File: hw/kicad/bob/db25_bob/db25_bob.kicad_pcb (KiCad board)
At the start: 2 copper layers, 4 parts, among them J1 DB25, U1 ADuM1200WU, U2 ADuM1200WU, U3 ADuM1200WU

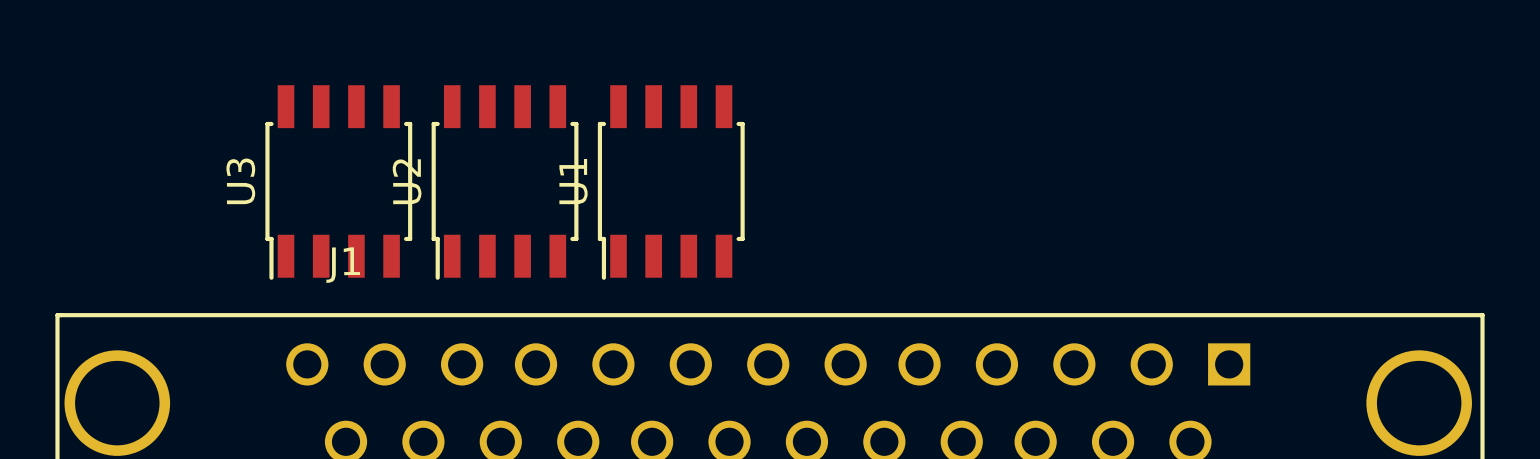
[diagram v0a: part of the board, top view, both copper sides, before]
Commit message: Added more isolators.
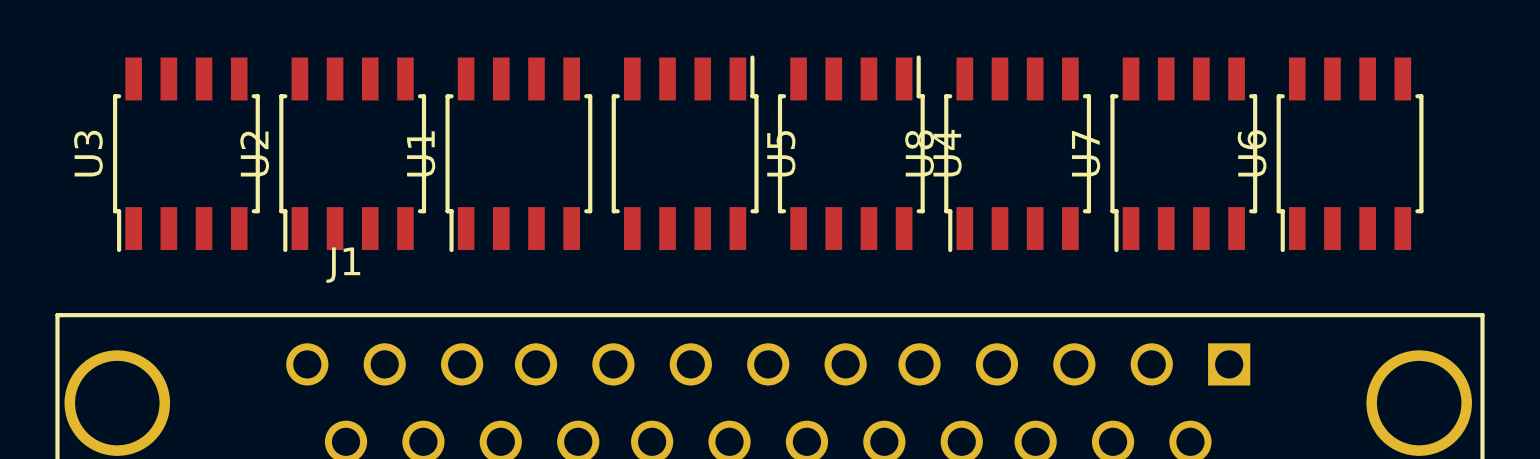
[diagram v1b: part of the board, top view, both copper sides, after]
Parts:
- added U4: ADuM1200WU, Housings_SOIC:SOIC-8_3.9x4.9mm_Pitch1.27mm, F.Cu at (154.0, 123.0)
- added U5: ADuM1200WU, Housings_SOIC:SOIC-8_3.9x4.9mm_Pitch1.27mm, F.Cu at (148.0, 123.0)
- added U6: ADuM1201WT, Housings_SOIC:SOIC-8_3.9x4.9mm_Pitch1.27mm, F.Cu at (172.0, 123.0)
- added U7: ADuM1201WT, Housings_SOIC:SOIC-8_3.9x4.9mm_Pitch1.27mm, F.Cu at (166.0, 123.0)
- added U8: ADuM1201WT, Housings_SOIC:SOIC-8_3.9x4.9mm_Pitch1.27mm, F.Cu at (160.0, 123.0)
- moved U1 5.59 mm to (142.0, 123.0)
- moved U2 5.59 mm to (136.0, 123.0)
- moved U3 5.59 mm to (130.0, 123.0)
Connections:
- U1 pad 5: Net-(U1-Pad5) -> GNDA
- U1 pad 8: Net-(U1-Pad8) -> +5VA
- U2 pad 5: Net-(U2-Pad5) -> GNDA
- U2 pad 8: Net-(U2-Pad8) -> +5VA
- U3 pad 5: Net-(U3-Pad5) -> GNDA
- U3 pad 8: Net-(U3-Pad8) -> +5VA

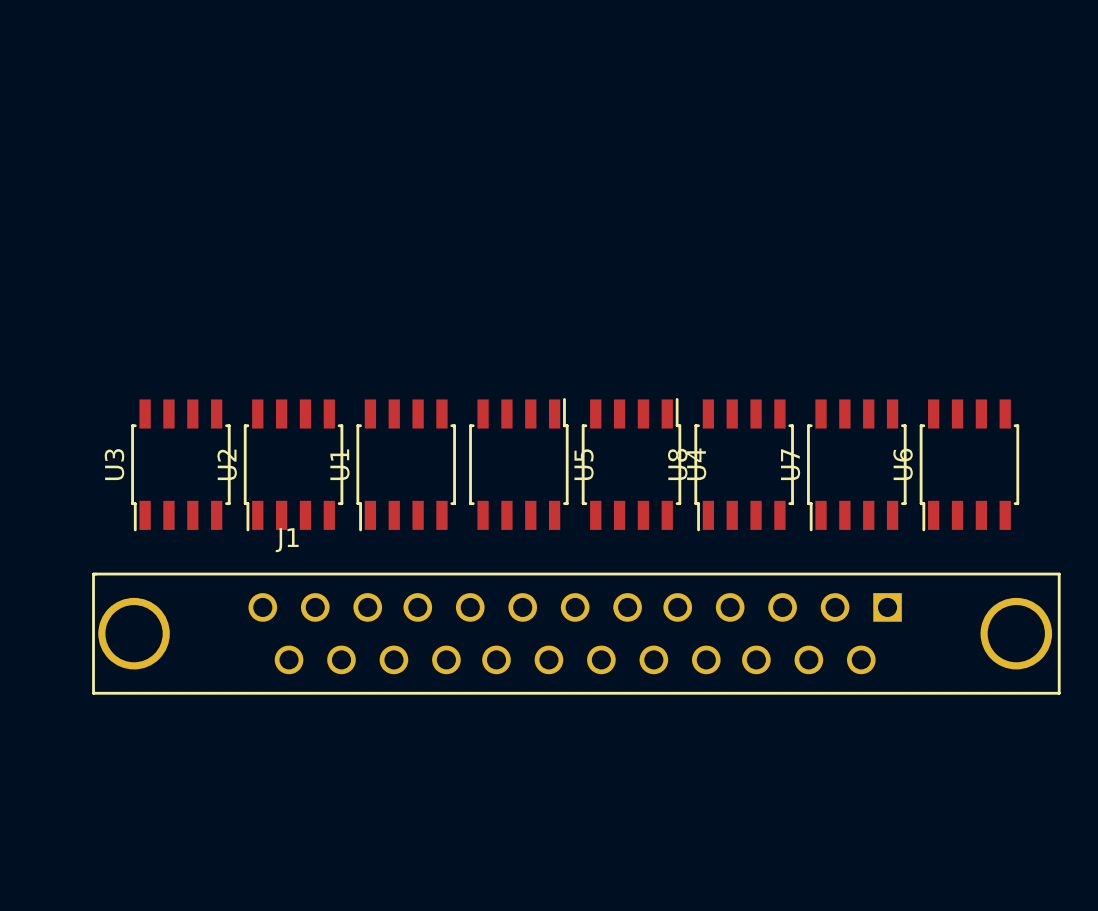
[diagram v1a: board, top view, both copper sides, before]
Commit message: Changed schematic to current feature set.
The bob will use two connections to the Mesa hardware and break out 5 SSerial
connections, 4 ABZ encoder interfaces, 5 inputs and 5 outputs.
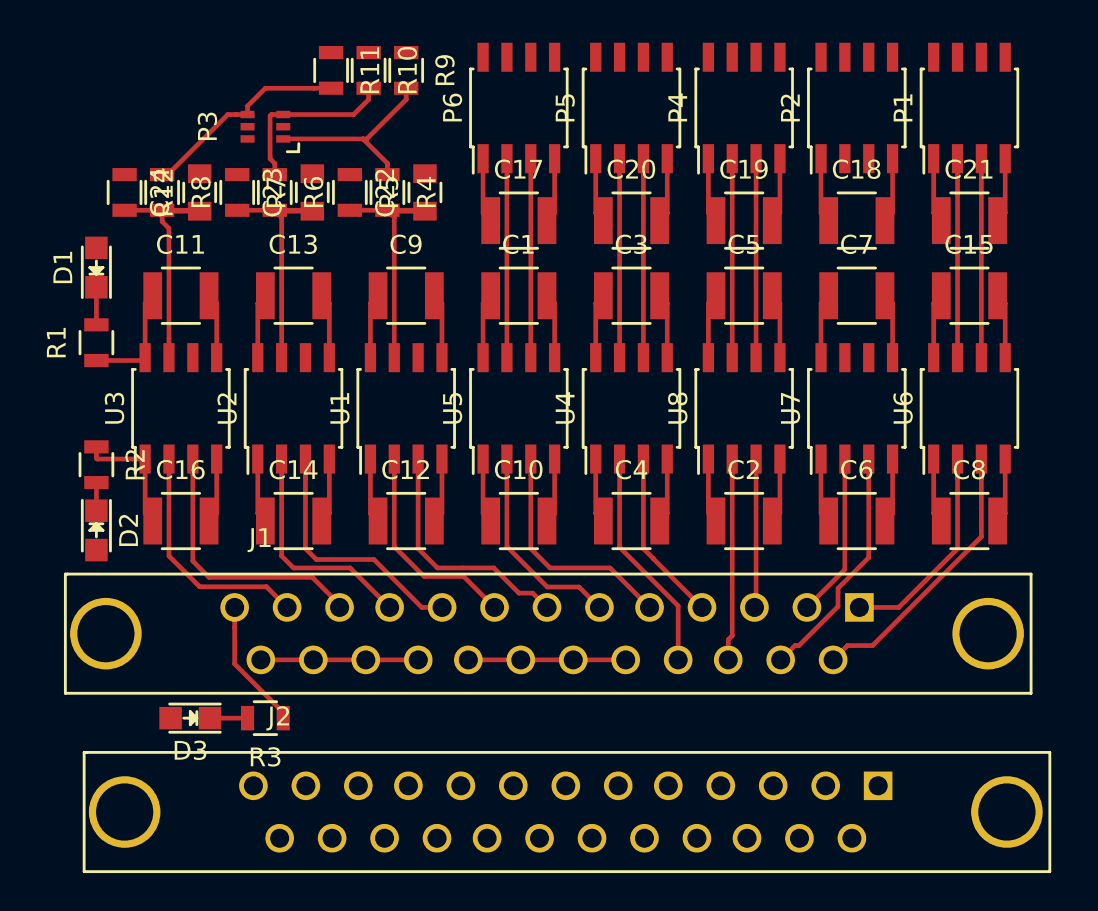
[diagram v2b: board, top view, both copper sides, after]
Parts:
- added C1: C, Capacitors_SMD:C_1210, F.Cu at (148.0, 114.0)
- added C10: C, Capacitors_SMD:C_1210, F.Cu at (148.0, 126.0)
- added C11: C, Capacitors_SMD:C_1210, F.Cu at (130.0, 114.0)
- added C12: C, Capacitors_SMD:C_1210, F.Cu at (142.0, 126.0)
- added C13: C, Capacitors_SMD:C_1210, F.Cu at (136.0, 114.0)
- added C14: C, Capacitors_SMD:C_1210, F.Cu at (136.0, 126.0)
- added C15: C, Capacitors_SMD:C_1210, F.Cu at (172.0, 114.0)
- added C16: C, Capacitors_SMD:C_1210, F.Cu at (130.0, 126.0)
- added C17: C, Capacitors_SMD:C_1210, F.Cu at (148.0, 110.0)
- added C18: C, Capacitors_SMD:C_1210, F.Cu at (166.0, 110.0)
- added C19: C, Capacitors_SMD:C_1210, F.Cu at (160.0, 110.0)
- added C2: C, Capacitors_SMD:C_1210, F.Cu at (160.0, 126.0)
- added C20: C, Capacitors_SMD:C_1210, F.Cu at (154.0, 110.0)
- added C21: C, Capacitors_SMD:C_1210, F.Cu at (172.0, 110.0)
- added C22: C, Capacitors_SMD:C_0805, F.Cu at (143.0, 108.5)
- added C23: C, Capacitors_SMD:C_0805, F.Cu at (137.0, 108.5)
- added C24: C, Capacitors_SMD:C_0805, F.Cu at (131.0, 108.5)
- added C3: C, Capacitors_SMD:C_1210, F.Cu at (154.0, 114.0)
- added C4: C, Capacitors_SMD:C_1210, F.Cu at (154.0, 126.0)
- added C5: C, Capacitors_SMD:C_1210, F.Cu at (160.0, 114.0)
- added C6: C, Capacitors_SMD:C_1210, F.Cu at (166.0, 126.0)
- added C7: C, Capacitors_SMD:C_1210, F.Cu at (166.0, 114.0)
- added C8: C, Capacitors_SMD:C_1210, F.Cu at (172.0, 126.0)
- added C9: C, Capacitors_SMD:C_1210, F.Cu at (142.0, 114.0)
- added D1: LED, LEDs:LED-0805, F.Cu at (125.5, 112.5)
- added D2: LED, LEDs:LED-0805, F.Cu at (125.5, 126.5)
- added D3: LED, LEDs:LED-0805, F.Cu at (130.5, 136.5)
- added J2: DB25, Connect:DB25FD, F.Cu at (150.5, 141.5)
- added P1: DIL8, Housings_SOIC:SOIC-8_3.9x4.9mm_Pitch1.27mm, F.Cu at (172.0, 104.0)
- added P2: DIL8, Housings_SOIC:SOIC-8_3.9x4.9mm_Pitch1.27mm, F.Cu at (166.0, 104.0)
- added P3: DIL6, Housings_SOT-23_SOT-143_TSOT-6:SC-70-6, F.Cu at (134.5, 105.0)
- added P4: DIL8, Housings_SOIC:SOIC-8_3.9x4.9mm_Pitch1.27mm, F.Cu at (160.0, 104.0)
- added P5: DIL8, Housings_SOIC:SOIC-8_3.9x4.9mm_Pitch1.27mm, F.Cu at (154.0, 104.0)
- added P6: DIL8, Housings_SOIC:SOIC-8_3.9x4.9mm_Pitch1.27mm, F.Cu at (148.0, 104.0)
- added R1: R, Resistors_SMD:R_0805, F.Cu at (125.5, 116.5)
- added R10: R, Resistors_SMD:R_0805, F.Cu at (140.0, 102.0)
- added R11: R, Resistors_SMD:R_0805, F.Cu at (138.0, 102.0)
- added R12: R, Resistors_SMD:R_0805, F.Cu at (127.0, 108.5)
- added R2: R, Resistors_SMD:R_0805, F.Cu at (125.5, 123.0)
- added R3: R, Resistors_SMD:R_0805, F.Cu at (134.5, 136.5)
- added R4: R, Resistors_SMD:R_0805, F.Cu at (141.0, 108.5)
- added R5: R, Resistors_SMD:R_0805, F.Cu at (139.0, 108.5)
- added R6: R, Resistors_SMD:R_0805, F.Cu at (135.0, 108.5)
- added R7: R, Resistors_SMD:R_0805, F.Cu at (133.0, 108.5)
- added R8: R, Resistors_SMD:R_0805, F.Cu at (129.0, 108.5)
- added R9: R, Resistors_SMD:R_0805, F.Cu at (142.0, 102.0)
- U1, U2, U3, U4, U5: value ADuM1200WU -> ADuM1201WT
- moved U1 3.00 mm to (142.0, 120.0)
- moved U2 3.00 mm to (136.0, 120.0)
- moved U3 3.00 mm to (130.0, 120.0)
- moved U4 3.00 mm to (154.0, 120.0), turned to 90 degrees
- moved U5 3.00 mm to (148.0, 120.0), turned to 90 degrees
- moved U6 3.00 mm to (172.0, 120.0)
- moved U7 3.00 mm to (166.0, 120.0)
- moved U8 3.00 mm to (160.0, 120.0)
- moved J1 1.50 mm to (149.5, 132.0)
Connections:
- net Net-(U1-Pad6) renamed OUT0
- net Net-(U2-Pad6) renamed OUT1
- net Net-(U3-Pad6) renamed OUT2
- U1 pad 2: IO12 -> IO11
- U1 pad 3: IO11 -> IO10
- U1 pad 7: Net-(U1-Pad7) -> IN0P
- U2 pad 2: IO14 -> IO13
- U2 pad 3: IO13 -> IO12
- U2 pad 7: Net-(U2-Pad7) -> IN1P
- U3 pad 2: IO16 -> IO15
- U3 pad 3: IO15 -> IO14
- U3 pad 7: Net-(U3-Pad7) -> IN2P
- U4 pad 1: +5VA -> +5V
- U4 pad 2: Net-(U4-Pad2) -> IO7
- U4 pad 3: Net-(U4-Pad3) -> IO6
- U4 pad 4: GNDA -> GND
- U4 pad 5: GND -> GNDA
- U4 pad 6: IO8 -> 3TX
- U4 pad 7: IO7 -> 3RX
- U4 pad 8: +5V -> +5VA
- U5 pad 1: +5VA -> +5V
- U5 pad 2: Net-(U5-Pad2) -> IO9
- U5 pad 3: Net-(U5-Pad3) -> IO8
- U5 pad 4: GNDA -> GND
- U5 pad 5: GND -> GNDA
- U5 pad 6: IO10 -> 4TX
- U5 pad 7: IO9 -> 4RX
- U5 pad 8: +5V -> +5VA
- U6 pad 2: IO1 -> IO0
- U6 pad 3: IO0 -> IO1
- U6 pad 6: Net-(U6-Pad6) -> 0TX
- U6 pad 7: Net-(U6-Pad7) -> 0RX
- U7 pad 2: IO3 -> IO2
- U7 pad 3: IO2 -> IO3
- U7 pad 6: Net-(U7-Pad6) -> 1TX
- U7 pad 7: Net-(U7-Pad7) -> 1RX
- U8 pad 2: IO4 -> IO5
- U8 pad 3: IO5 -> IO4
- U8 pad 6: Net-(U8-Pad6) -> 2TX
- U8 pad 7: Net-(U8-Pad7) -> 2RX
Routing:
- net +5VA: track 0.00 -> 47.7 mm
- net GNDA: track 0.00 -> 45.1 mm
- net +5V: track 0.00 -> 38.8 mm
- net GND: track 0.00 -> 36.1 mm
- net IO1: track 0.00 -> 14.7 mm
- net IO14: track 0.00 -> 14.4 mm
- net IN1P: track 0.00 -> 14.0 mm
- net IN0P: track 0.00 -> 14.0 mm
- net IN2P: track 0.00 -> 14.0 mm
- net IO10: track 0.00 -> 13.4 mm
- net IO12: track 0.00 -> 13.3 mm
- net IO3: track 0.00 -> 12.8 mm
- net IO15: track 0.00 -> 12.6 mm
- net IO8: track 0.00 -> 12.4 mm
- net IO13: track 0.00 -> 12.1 mm
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
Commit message: Forgot traces.
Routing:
- net 1TX: track 0.00 -> 10.6 mm
- net 1RX: track 0.00 -> 10.6 mm
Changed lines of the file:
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@@
     (thickness 1.6)
     (drawings 0)
-    (tracks 221)
+    (tracks 223)
     (zones 0)
     (modules 55)
@@
   (segment (start 171.365 117.3) (end 171.365 106.7) (width 0.25) (layer F.Cu) (net 53))
   (segment (start 172.635 117.3) (end 172.635 106.7) (width 0.25) (layer F.Cu) (net 54))
+  (segment (start 165.365 117.3) (end 165.365 106.7) (width 0.25) (layer F.Cu) (net 57))
+  (segment (start 166.635 106.7) (end 166.635 117.3) (width 0.25) (layer F.Cu) (net 58))
   (segment (start 139.70024 105.65024) (end 139.89976 105.65024) (width 0.25) (layer F.Cu) (net 61))
   (segment (start 139.89976 105.65024) (end 142 103.55) (width 0.25) (layer F.Cu) (net 61))

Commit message: Latest changes.
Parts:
- added C25: C, Capacitors_SMD:C_1210, F.Cu at (199.5, 87.0)
- added C26: C, Capacitors_SMD:C_1210, F.Cu at (211.5, 87.0)
- added C27: C, Capacitors_SMD:C_1210, F.Cu at (199.5, 93.0)
- added C28: C, Capacitors_SMD:C_1210, F.Cu at (211.5, 93.0)
- added C29: C, Capacitors_SMD:C_1210, F.Cu at (199.5, 99.0)
- added C30: C, Capacitors_SMD:C_1210, F.Cu at (211.5, 99.0)
- added C31: C, Capacitors_SMD:C_1210, F.Cu at (199.5, 105.0)
- added C32: C, Capacitors_SMD:C_1210, F.Cu at (211.5, 105.0)
- added C33: C, Capacitors_SMD:C_1210, F.Cu at (199.5, 111.0)
- added C34: C, Capacitors_SMD:C_1210, F.Cu at (211.5, 111.0)
- added C35: C, Capacitors_SMD:C_1210, F.Cu at (199.5, 117.0)
- added C36: C, Capacitors_SMD:C_1210, F.Cu at (211.5, 117.0)
- added C37: C, Capacitors_SMD:C_1210, B.Cu at (215.0, 81.5)
- added C38: C, Capacitors_SMD:C_1210, B.Cu at (218.5, 106.0)
- added C39: C, Capacitors_SMD:C_1210, B.Cu at (218.5, 118.0)
- added J3: RJ45, Connect:RJ45_8, F.Cu at (235.5, 81.0)
- added J4: RJ45, Connect:RJ45_8, F.Cu at (235.5, 97.5)
- added J5: RJ45, Connect:RJ45_8, F.Cu at (235.5, 114.0)
- added J6: RJ45, Connect:RJ45_8, F.Cu at (235.5, 130.5)
- added P7: DIL16, Housings_SOIC:SOIC-16_3.9x9.9mm_Pitch1.27mm, F.Cu at (219.0, 88.5)
- added P8: DIL16, Housings_SOIC:SOIC-16_3.9x9.9mm_Pitch1.27mm, F.Cu at (218.5, 106.0)
- added P9: DIL16, Housings_SOIC:SOIC-16_3.9x9.9mm_Pitch1.27mm, F.Cu at (218.5, 118.0)
- added U10: ADuM1200CR, Housings_SOIC:SOIC-8_3.9x4.9mm_Pitch1.27mm, F.Cu at (205.5, 93.0)
- added U11: ADuM1200CR, Housings_SOIC:SOIC-8_3.9x4.9mm_Pitch1.27mm, F.Cu at (205.5, 99.0)
- added U12: ADuM1200CR, Housings_SOIC:SOIC-8_3.9x4.9mm_Pitch1.27mm, F.Cu at (205.5, 105.0)
- added U13: ADuM1200CR, Housings_SOIC:SOIC-8_3.9x4.9mm_Pitch1.27mm, F.Cu at (205.5, 111.0)
- added U14: ADuM1200CR, Housings_SOIC:SOIC-8_3.9x4.9mm_Pitch1.27mm, F.Cu at (205.5, 117.0)
- added U9: ADuM1200CR, Housings_SOIC:SOIC-8_3.9x4.9mm_Pitch1.27mm, F.Cu at (205.5, 87.0)
- moved D3 56.7 mm to (186.0, 125.0), turned to 270 degrees
- moved J2 53.9 mm to (191.0, 106.0), turned to 90 degrees
- moved R3 53.8 mm to (186.0, 121.0), turned to 270 degrees
- moved D2 50.6 mm to (176.0, 130.0), turned to 0 degrees
- moved R2 47.5 mm to (172.5, 130.0), turned to 0 degrees
- moved C16 45.5 mm to (175.5, 125.5), turned to 90 degrees
- moved R1 42.7 mm to (166.0, 130.0), turned to 180 degrees
- moved C8 42.6 mm to (175.5, 83.5), turned to 90 degrees
- moved J1 41.2 mm to (181.5, 106.0), turned to 90 degrees
- moved D1 40.9 mm to (162.5, 130.0), turned to 180 degrees
- moved C14 40.0 mm to (175.5, 119.5), turned to 90 degrees
- moved U3 39.9 mm to (169.5, 125.5), turned to 180 degrees
- moved C6 37.7 mm to (175.5, 89.5), turned to 90 degrees
- moved R12 36.9 mm to (158.0, 128.5), turned to 0 degrees
- moved U6 36.6 mm to (169.5, 83.5), turned to 180 degrees
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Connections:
- net GNDA renamed EN-
- J2 pad 1: Net-(J2-Pad1) -> ENC0BO
- J2 pad 14: Net-(J2-Pad14) -> ENC0AO
- J2 pad 15: Net-(J2-Pad15) -> ENC0ZO
- J2 pad 16: Net-(J2-Pad16) -> ENC1BO
- J2 pad 17: Net-(J2-Pad17) -> ENC2AO
- J2 pad 18: Net-(J2-Pad18) -> GND
- J2 pad 19: Net-(J2-Pad19) -> GND
- J2 pad 2: Net-(J2-Pad2) -> ENC1AO
- J2 pad 20: Net-(J2-Pad20) -> GND
- J2 pad 21: Net-(J2-Pad21) -> GND
- J2 pad 22: Net-(J2-Pad22) -> +5V
- J2 pad 23: Net-(J2-Pad23) -> +5V
- J2 pad 24: Net-(J2-Pad24) -> +5V
- J2 pad 25: Net-(J2-Pad25) -> +5V
- J2 pad 3: Net-(J2-Pad3) -> ENC1ZO
- J2 pad 4: Net-(J2-Pad4) -> ENC2BO
- J2 pad 5: Net-(J2-Pad5) -> ENC3AO
- J2 pad 6: Net-(J2-Pad6) -> ENC2ZO
- J2 pad 7: Net-(J2-Pad7) -> ENC3ZO
- J2 pad 8: Net-(J2-Pad8) -> ENC3BO
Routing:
- net EN-: track 45.1 -> 104.0 mm
- net ENC1B-: track 0.00 -> 37.3 mm
- net ENC3A-: track 0.00 -> 34.1 mm
- net ENC1B+: track 0.00 -> 33.7 mm
- net ENC0Z-: track 0.00 -> 27.8 mm
- net ENC3A+: track 0.00 -> 26.9 mm
- net ENC0Z+: track 0.00 -> 26.5 mm
- net ENC3Z-: track 0.00 -> 25.2 mm
- net ENC3B+: track 0.00 -> 21.3 mm
- net GND: track 36.1 -> 56.9 mm
- net ENC3ZO: track 0.00 -> 20.4 mm
- net ENC1Z+: track 0.00 -> 20.3 mm
- net ENC3BO: track 0.00 -> 19.9 mm
- net ENC2A+: track 0.00 -> 19.9 mm
- net ENC3AO: track 0.00 -> 18.6 mm
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- added copper zone on F.Cu, net +5V
- added copper zone on F.Cu, net +5VA
- added copper zone on B.Cu, net EN-
- added copper zone on B.Cu, net GND
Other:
- board outline added: 98 x 72 mm
